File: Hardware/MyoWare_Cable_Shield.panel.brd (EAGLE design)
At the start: 52.1 x 20.7 mm, 18 parts

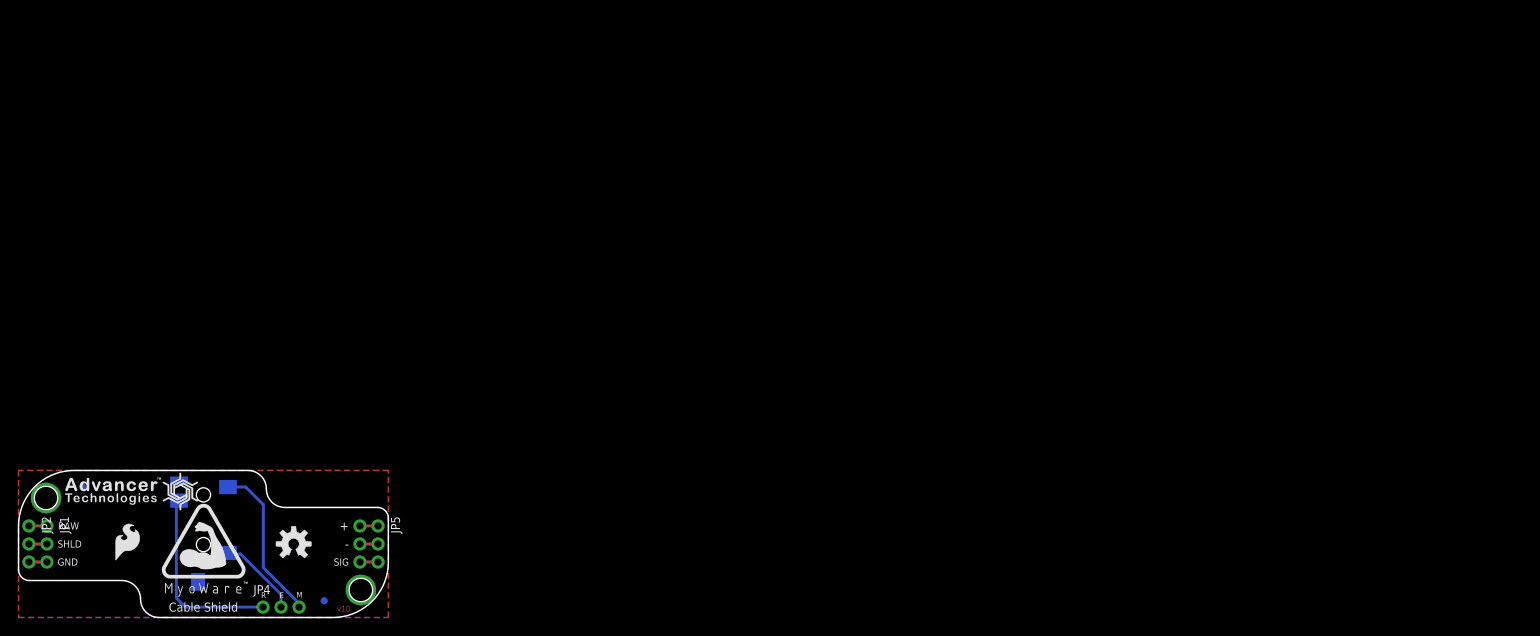
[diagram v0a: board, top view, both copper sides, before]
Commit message: Cleaned up dimension symmetry & started a panel
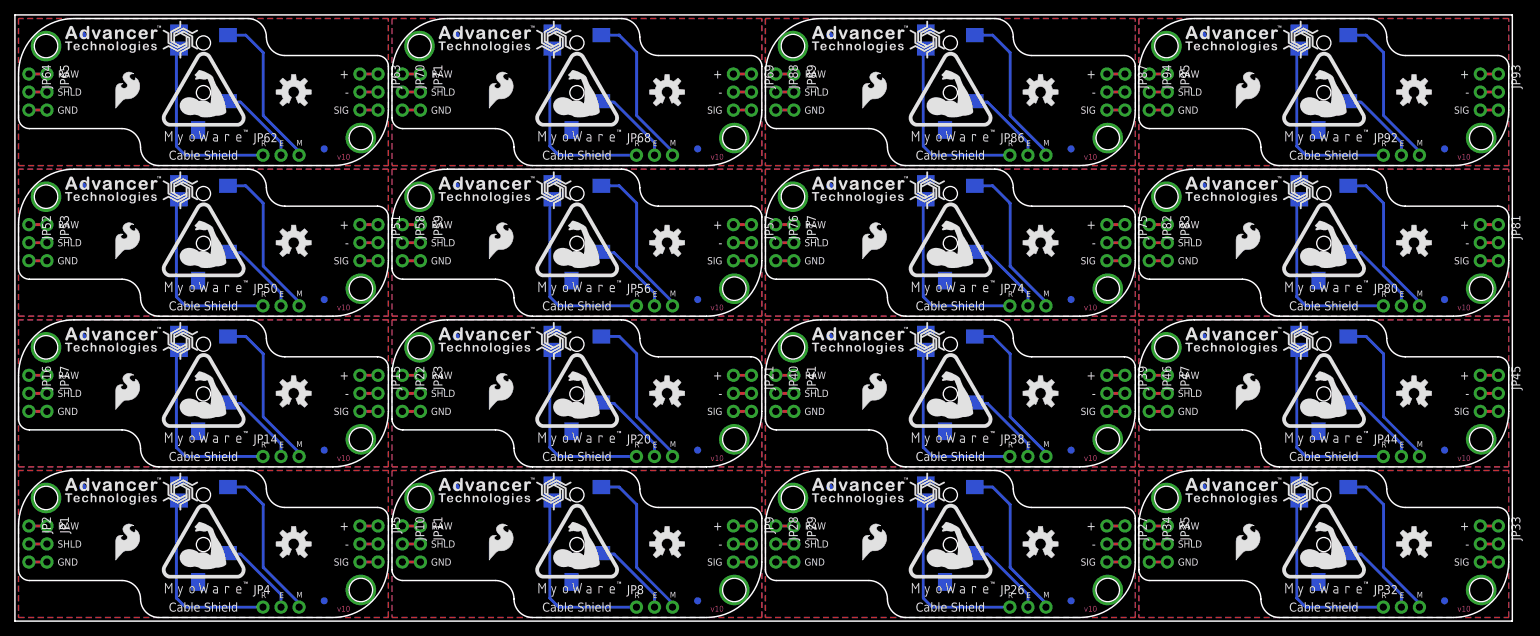
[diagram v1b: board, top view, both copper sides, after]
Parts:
- added FID10, FID11, FID12, FID13, FID14, FID15, FID16, FID17, FID18, FID19, FID20, FID21, FID22, FID23, FID24, FID25, FID26, FID27, FID28, FID29, FID3, FID30, FID31, FID32, FID4, FID5, FID6, FID7, FID8, FID9: FIDUCIAL1X2, SparkFun-Aesthetics:FIDUCIAL-1X2
- added JP10, JP11, JP13, JP14, JP15, JP16, JP17, JP19, JP20, JP21, JP22, JP23, JP25, JP26, JP27, JP28, JP29, JP31, JP32, JP33, JP34, JP35, JP37, JP38, JP39, JP40, JP41, JP43, JP44, JP45, JP46, JP47, JP49, JP50, JP51, JP52, JP53, JP55, JP56, JP57, JP58, JP59, JP61, JP62, JP63, JP64, JP65, JP67, JP68, JP69, JP7, JP70, JP71, JP73, JP74, JP75, JP76, JP77, JP79, JP8, JP80, JP81, JP82, JP83, JP85, JP86, JP87, JP88, JP89, JP9, JP91, JP92, JP93, JP94, JP95: Power, SparkFun-Connectors:1X03_NO_SILK
- added JP12, JP18, JP24, JP30, JP36, JP42, JP48, JP54, JP60, JP66, JP72, JP78, JP84, JP90, JP96: 3.5mm Jack, SparkFun-Connectors:AUDIO-JACK-3.5MM-SMD
- added LOGO10, LOGO13, LOGO16, LOGO19, LOGO22, LOGO25, LOGO28, LOGO31, LOGO34, LOGO37, LOGO4, LOGO40, LOGO43, LOGO46, LOGO7: OSHW-LOGOM, SparkFun-Aesthetics:OSHW-LOGO-M
- added LOGO11, LOGO14, LOGO17, LOGO20, LOGO23, LOGO26, LOGO29, LOGO32, LOGO35, LOGO38, LOGO41, LOGO44, LOGO47, LOGO5, LOGO8: SFE_LOGO_FLAME.2_INCH, SparkFun-Aesthetics:SFE_LOGO_FLAME_.2
- added LOGO12, LOGO15, LOGO18, LOGO21, LOGO24, LOGO27, LOGO3, LOGO30, LOGO33, LOGO36, LOGO39, LOGO42, LOGO45, LOGO6, LOGO9: (no value), advancer-technologies:MYOWARE_LOGO
- added SPIRAL1, SPIRAL10, SPIRAL11, SPIRAL12, SPIRAL13, SPIRAL14, SPIRAL15, SPIRAL2, SPIRAL3, SPIRAL4, SPIRAL5, SPIRAL6, SPIRAL7, SPIRAL8, SPIRAL9: (no value), advancer-technologies:SPIRAL_LOGO_60%
- added STANDOFF10, STANDOFF11, STANDOFF12, STANDOFF13, STANDOFF14, STANDOFF15, STANDOFF16, STANDOFF17, STANDOFF18, STANDOFF19, STANDOFF20, STANDOFF21, STANDOFF22, STANDOFF23, STANDOFF24, STANDOFF25, STANDOFF26, STANDOFF27, STANDOFF28, STANDOFF29, STANDOFF3, STANDOFF30, STANDOFF31, STANDOFF32, STANDOFF4, STANDOFF5, STANDOFF6, STANDOFF7, STANDOFF8, STANDOFF9: STAND-OFF, SparkFun-Electromechanical:STAND-OFF
- added U$1, U$10, U$13, U$16, U$19, U$22, U$25, U$28, U$31, U$34, U$37, U$40, U$43, U$46, U$7: (no value), SparkFun-Aesthetics:NO_PB_LOGO_0.120
- added U$11, U$14, U$17, U$2, U$20, U$23, U$26, U$29, U$32, U$35, U$38, U$41, U$44, U$47, U$8: (no value), advancer-technologies:ADVANCER_LOGO
- added U$12, U$15, U$18, U$21, U$24, U$27, U$30, U$33, U$36, U$39, U$4, U$42, U$45, U$48, U$9: (no value), SparkFun-Aesthetics:ROHS_LOGO_0.18_IN
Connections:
- new net END1: JP12.TIP, JP8.2
- new net END10: JP62.2, JP66.TIP
- new net END11: JP68.2, JP72.TIP
- new net END12: JP74.2, JP78.TIP
- new net END13: JP80.2, JP84.TIP
- new net END14: JP86.2, JP90.TIP
- new net END15: JP92.2, JP96.TIP
- new net END2: JP14.2, JP18.TIP
- new net END3: JP20.2, JP24.TIP
- new net END4: JP26.2, JP30.TIP
- new net END5: JP32.2, JP36.TIP
- new net END6: JP38.2, JP42.TIP
- new net END7: JP44.2, JP48.TIP
- new net END8: JP50.2, JP54.TIP
- new net END9: JP56.2, JP60.TIP
- new net GND1: JP10.3, JP11.3, JP7.2, JP9.2
- new net GND10: JP61.2, JP63.2, JP64.3, JP65.3
- new net GND11: JP67.2, JP69.2, JP70.3, JP71.3
- new net GND12: JP73.2, JP75.2, JP76.3, JP77.3
- new net GND13: JP79.2, JP81.2, JP82.3, JP83.3
- new net GND14: JP85.2, JP87.2, JP88.3, JP89.3
- new net GND15: JP91.2, JP93.2, JP94.3, JP95.3
- new net GND2: JP13.2, JP15.2, JP16.3, JP17.3
- new net GND3: JP19.2, JP21.2, JP22.3, JP23.3
- new net GND4: JP25.2, JP27.2, JP28.3, JP29.3
- new net GND5: JP31.2, JP33.2, JP34.3, JP35.3
- new net GND6: JP37.2, JP39.2, JP40.3, JP41.3
- new net GND7: JP43.2, JP45.2, JP46.3, JP47.3
- new net GND8: JP49.2, JP51.2, JP52.3, JP53.3
- new net GND9: JP55.2, JP57.2, JP58.3, JP59.3
- new net MID1: JP12.SLEEVE, JP8.3
- new net MID10: JP62.3, JP66.SLEEVE
- new net MID11: JP68.3, JP72.SLEEVE
- new net MID12: JP74.3, JP78.SLEEVE
- new net MID13: JP80.3, JP84.SLEEVE
- new net MID14: JP86.3, JP90.SLEEVE
- new net MID15: JP92.3, JP96.SLEEVE
- new net MID2: JP14.3, JP18.SLEEVE
- new net MID3: JP20.3, JP24.SLEEVE
- new net MID4: JP26.3, JP30.SLEEVE
- new net MID5: JP32.3, JP36.SLEEVE
- new net MID6: JP38.3, JP42.SLEEVE
- new net MID7: JP44.3, JP48.SLEEVE
- new net MID8: JP50.3, JP54.SLEEVE
- new net MID9: JP56.3, JP60.SLEEVE
- new net RAW1: JP10.1, JP11.1
- new net RAW10: JP64.1, JP65.1
- new net RAW11: JP70.1, JP71.1
- new net RAW12: JP76.1, JP77.1
- new net RAW13: JP82.1, JP83.1
- new net RAW14: JP88.1, JP89.1
- new net RAW15: JP94.1, JP95.1
- new net RAW2: JP16.1, JP17.1
- new net RAW3: JP22.1, JP23.1
- new net RAW4: JP28.1, JP29.1
- new net RAW5: JP34.1, JP35.1
- new net RAW6: JP40.1, JP41.1
- new net RAW7: JP46.1, JP47.1
- new net RAW8: JP52.1, JP53.1
- new net RAW9: JP58.1, JP59.1
- new net SHIELD1: JP10.2, JP11.2
- new net SHIELD10: JP64.2, JP65.2
- new net SHIELD11: JP70.2, JP71.2
- new net SHIELD12: JP76.2, JP77.2
- new net SHIELD13: JP82.2, JP83.2
- new net SHIELD14: JP88.2, JP89.2
- new net SHIELD15: JP94.2, JP95.2
- new net SHIELD2: JP16.2, JP17.2
- new net SHIELD3: JP22.2, JP23.2
- new net SHIELD4: JP28.2, JP29.2
- new net SHIELD5: JP34.2, JP35.2
- new net SHIELD6: JP40.2, JP41.2
- new net SHIELD7: JP46.2, JP47.2
- new net SHIELD8: JP52.2, JP53.2
- new net SHIELD9: JP58.2, JP59.2
- new net SIG1: JP7.3, JP9.3
- new net SIG10: JP61.3, JP63.3
- new net SIG11: JP67.3, JP69.3
- new net SIG12: JP73.3, JP75.3
- new net SIG13: JP79.3, JP81.3
- new net SIG14: JP85.3, JP87.3
- new net SIG15: JP91.3, JP93.3
- new net SIG2: JP13.3, JP15.3
- new net SIG3: JP19.3, JP21.3
- new net SIG4: JP25.3, JP27.3
- new net SIG5: JP31.3, JP33.3
- new net SIG6: JP37.3, JP39.3
- new net SIG7: JP43.3, JP45.3
- new net SIG8: JP49.3, JP51.3
- new net SIG9: JP55.3, JP57.3
- new net VCC1: JP7.1, JP9.1
- new net VCC10: JP61.1, JP63.1
- new net VCC11: JP67.1, JP69.1
- new net VCC12: JP73.1, JP75.1
- new net VCC13: JP79.1, JP81.1
- new net VCC14: JP85.1, JP87.1
- new net VCC15: JP91.1, JP93.1
- new net VCC2: JP13.1, JP15.1
- new net VCC3: JP19.1, JP21.1
- new net VCC4: JP25.1, JP27.1
- new net VCC5: JP31.1, JP33.1
- new net VCC6: JP37.1, JP39.1
- new net VCC7: JP43.1, JP45.1
- new net VCC8: JP49.1, JP51.1
- new net VCC9: JP55.1, JP57.1
- new net VREF1: JP12.RING, JP8.1
- new net VREF10: JP62.1, JP66.RING
- new net VREF11: JP68.1, JP72.RING
- new net VREF12: JP74.1, JP78.RING
- new net VREF13: JP80.1, JP84.RING
- new net VREF14: JP86.1, JP90.RING
- new net VREF15: JP92.1, JP96.RING
- new net VREF2: JP14.1, JP18.RING
- new net VREF3: JP20.1, JP24.RING
- new net VREF4: JP26.1, JP30.RING
- new net VREF5: JP32.1, JP36.RING
- new net VREF6: JP38.1, JP42.RING
- new net VREF7: JP44.1, JP48.RING
- new net VREF8: JP50.1, JP54.RING
- new net VREF9: JP56.1, JP60.RING
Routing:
- net VREF7: track 0.00 -> 26.7 mm
- net VREF5: track 0.00 -> 26.7 mm
- net VREF3: track 0.00 -> 26.7 mm
- net VREF15: track 0.00 -> 26.7 mm
- net VREF11: track 0.00 -> 26.7 mm
- net VREF10: track 0.00 -> 26.7 mm
- net VREF9: track 0.00 -> 26.7 mm
- net VREF8: track 0.00 -> 26.7 mm
- net VREF2: track 0.00 -> 26.7 mm
- net VREF13: track 0.00 -> 26.7 mm
- net VREF1: track 0.00 -> 26.7 mm
- net VREF6: track 0.00 -> 26.7 mm
- net VREF14: track 0.00 -> 26.7 mm
- net VREF4: track 0.00 -> 26.7 mm
- net VREF12: track 0.00 -> 26.7 mm
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- added copper zone on layer 1, net GND1
- added copper zone on layer 16, net GND1
- added copper zone on layer 1, net GND10
- added copper zone on layer 16, net GND10
- added copper zone on layer 1, net GND11
- added copper zone on layer 16, net GND11
- added copper zone on layer 1, net GND12
- added copper zone on layer 16, net GND12
- added copper zone on layer 1, net GND13
- added copper zone on layer 16, net GND13
- added copper zone on layer 1, net GND14
- added copper zone on layer 16, net GND14
- added copper zone on layer 1, net GND15
- added copper zone on layer 16, net GND15
- added copper zone on layer 1, net GND2
- added copper zone on layer 16, net GND2
- added copper zone on layer 1, net GND3
- added copper zone on layer 16, net GND3
- added copper zone on layer 1, net GND4
- added copper zone on layer 16, net GND4
- added copper zone on layer 1, net GND5
- added copper zone on layer 16, net GND5
- added copper zone on layer 1, net GND6
- added copper zone on layer 16, net GND6
- added copper zone on layer 1, net GND7
- added copper zone on layer 16, net GND7
- added copper zone on layer 1, net GND8
- added copper zone on layer 16, net GND8
- added copper zone on layer 1, net GND9
- added copper zone on layer 16, net GND9
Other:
- board size 52.1 x 20.7 mm -> 210.8 x 85.3 mm
